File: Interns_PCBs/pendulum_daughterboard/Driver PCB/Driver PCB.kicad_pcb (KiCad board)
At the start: 2 copper layers, 69.2 x 54 mm, 43 parts, among them IC1 AND GATES, IC2 NAND (Used as AND), IC3 NAND (Used as Inverter), IC4 OR, IC5 MAX9928FAUA+, J1 AVR-ISP-6, J2 Coil, J4 Conn_01x04, J5 DRIVE_GND, J7 DRIVE_5V_IN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

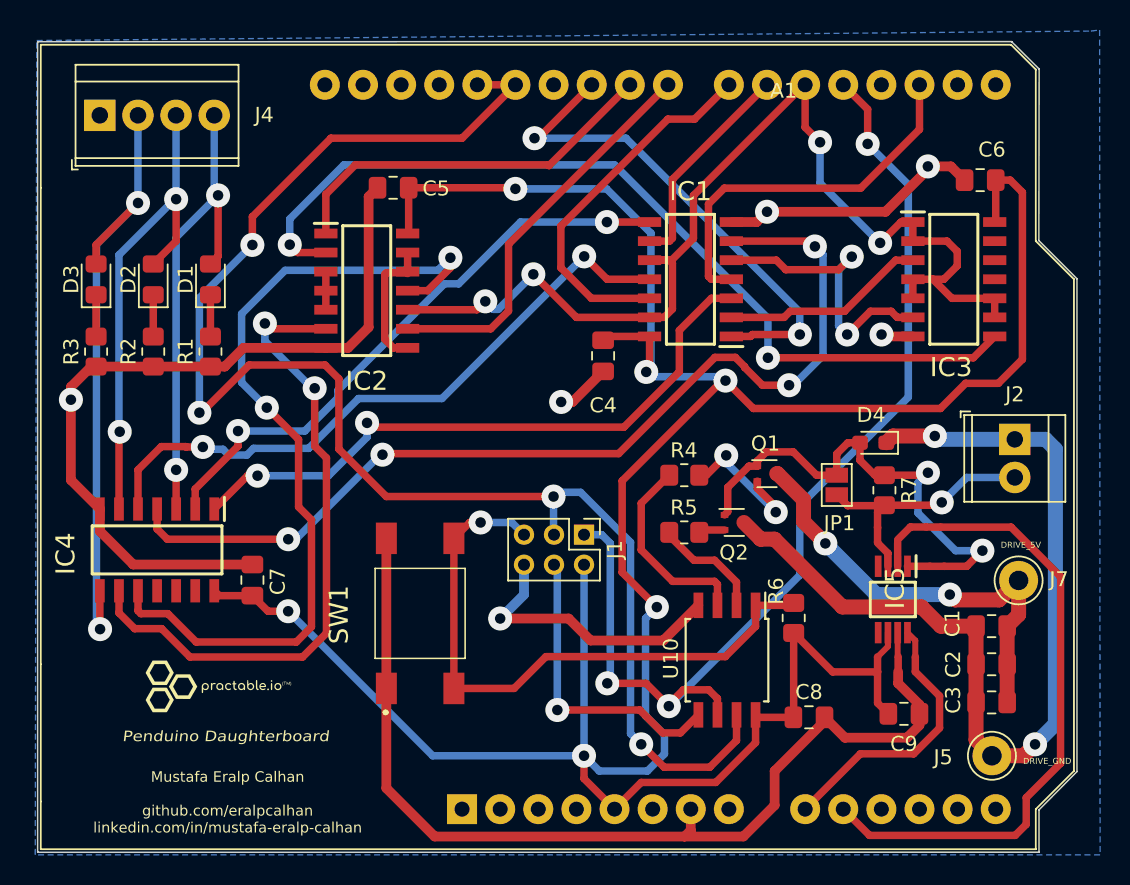
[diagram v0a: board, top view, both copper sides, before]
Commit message: Changed Diode
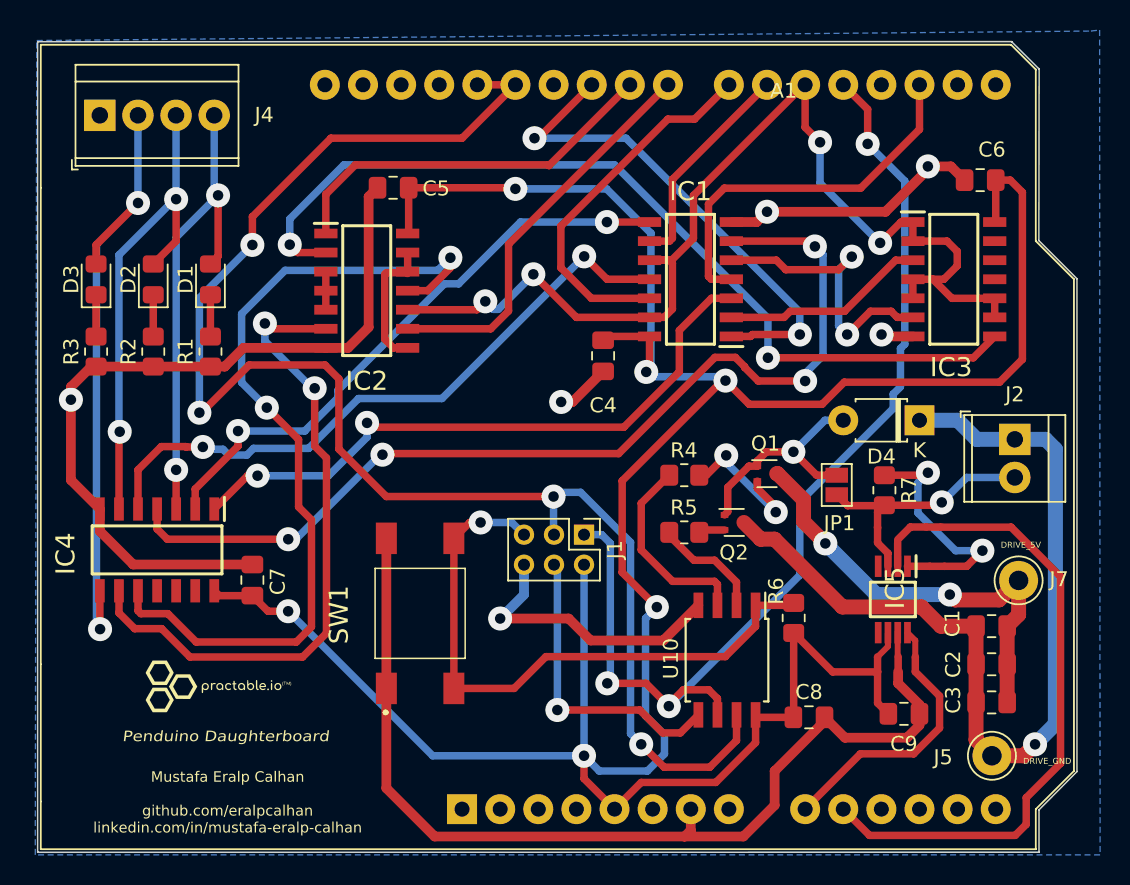
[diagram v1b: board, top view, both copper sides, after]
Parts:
- D4: footprint Diode_SMD:D_0603_1608Metric_Pad1.05x0.95mm_HandSolder -> Diode_THT:D_T-1_P5.08mm_Horizontal
- moved D4 3.43 mm to (149.9, 80.0)
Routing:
- net Net-(D4-Pad2): track 31.7 -> 29.4 mm, vias 2 -> 3
- net DRIVE_GND: track 62.6 -> 60.7 mm, vias 2 -> 1

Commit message: Changes with the Components
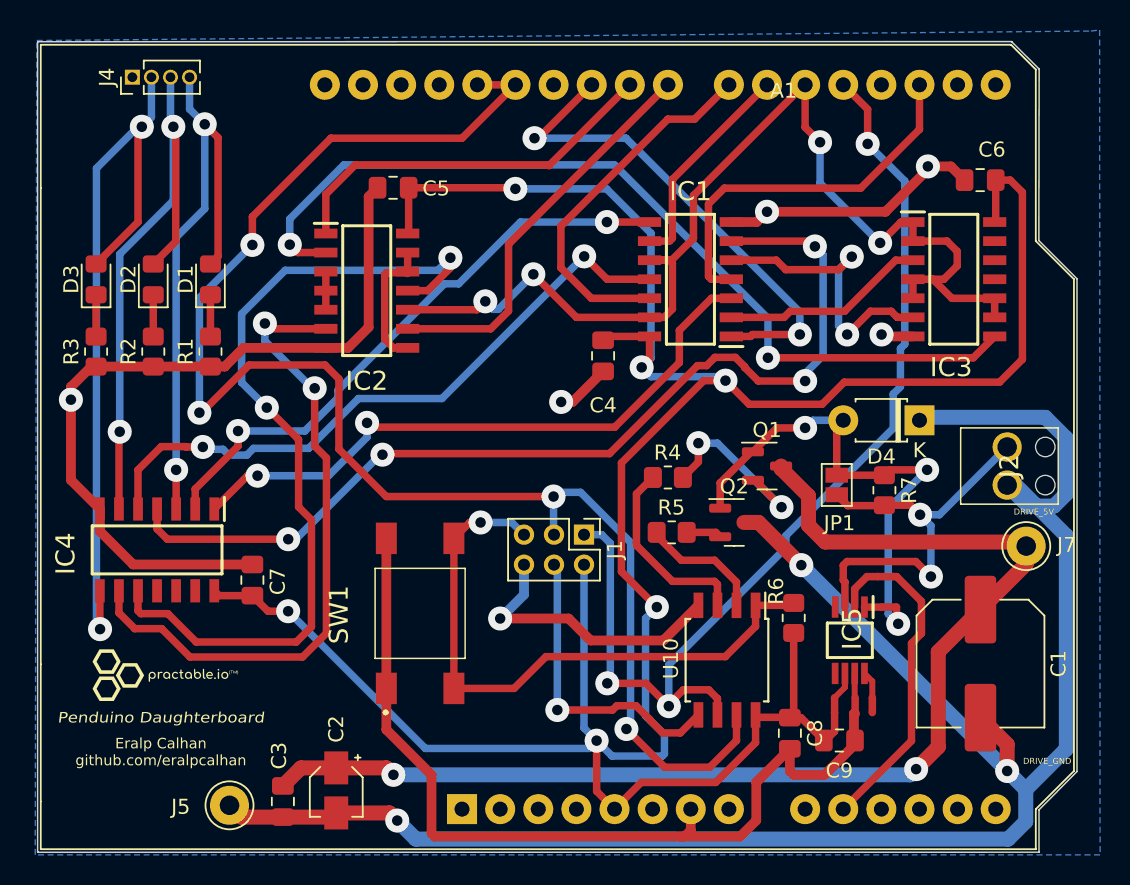
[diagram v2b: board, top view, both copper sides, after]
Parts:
- C1: value 460u -> 470u; footprint Capacitor_SMD:C_0805_2012Metric_Pad1.18x1.45mm_HandSolder -> Capacitor_SMD:C_Elec_8x10.2
- C2: footprint Capacitor_SMD:C_0805_2012Metric_Pad1.18x1.45mm_HandSolder -> Capacitor_SMD:CP_Elec_3x5.3
- J2: footprint TerminalBlock_TE-Connectivity:TerminalBlock_TE_282834-2_1x02_P2.54mm_Horizontal -> Connector_Molex:RSPROPenduinoTerminal
- J4: footprint TerminalBlock_TE-Connectivity:TerminalBlock_TE_282834-4_1x04_P2.54mm_Horizontal -> Connector_PinHeader_1.27mm:PinHeader_1x04_P1.27mm_Vertical
- Q1, Q2: footprint Package_TO_SOT_SMD:SOT-523 -> Package_TO_SOT_SMD:SOT-23
- moved J5 50.9 mm to (103.9, 105.7)
- moved C3 47.7 mm to (107.4, 105.4), turned to -90 degrees
- moved C2 44.5 mm to (111.0, 104.7), turned to -90 degrees
- moved C9 4.65 mm to (144.5, 101.3)
- moved NT3 4.62 mm to (147.6, 90.4)
- moved NT5 4.20 mm to (147.8, 92.5)
- moved NT1 3.95 mm to (144.2, 99.0)
- moved NT2 3.95 mm to (145.6, 99.0)
- moved NT6 3.95 mm to (146.7, 99.0)
- moved IC5 3.95 mm to (145.2, 94.7)
- moved G*** 3.62 mm to (99.6, 97.0)
- moved NT4 3.41 mm to (144.8, 90.2)
- moved J4 3.34 mm to (97.4, 57.1), turned to 90 degrees
- moved J2 3.09 mm to (155.7, 84.3), turned to 90 degrees
- moved C1 2.60 mm to (153.9, 96.2), turned to -90 degrees
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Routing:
- net DRIVE_GND: track 60.7 -> 129.6 mm, vias 1 -> 3
- net DRIVE_5V: track 29.4 -> 80.7 mm
- net CURRENT_SIGN_OUT: track 40.0 -> 18.6 mm
- net CURRENT_SENSE_OUT: track 15.6 -> 0.00 mm
- net Net-(J2-Pad2): track 14.6 -> 24.6 mm, vias 1 -> 2
- net OR_OUT_3: track 43.3 -> 51.1 mm
- net OR_OUT_1: track 32.3 -> 39.9 mm
- net OR_OUT_2: track 32.9 -> 39.9 mm
- net D_GND: track 160.2 -> 155.1 mm
- net Net-(D4-Pad2): track 29.4 -> 34.4 mm
- net D_5V: track 192.0 -> 188.2 mm
- net Net-(Q1-Pad2): track 10.1 -> 12.7 mm
- net LOAD_MCU: track 7.53 -> 8.36 mm
- net Net-(IC5-Pad2): track 3.83 -> 3.08 mm
- net Net-(Q2-Pad2): track 1.75 -> 2.35 mm
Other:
- board text added: "Eralp Calhan github.com/eralpcalhan"
- board text removed: "Mustafa Eralp Calhan github.com/eralpcalhan linkedin.com/in/mustafa-eralp-calhan"

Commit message: Friday Updates
24/06/22
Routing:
- net CURRENT_SENSE_OUT: track 0.00 -> 9.01 mm
- net D_GND: track 155.1 -> 153.7 mm
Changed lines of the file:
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@@
   (segment (start 95.25 87.400022) (end 97.468978 89.619) (width 0.65) (layer "F.Cu") (net 56))
   (segment (start 139.0142 66.802) (end 139.7 66.1162) (width 0.65) (layer "F.Cu") (net 56))
+  (segment (start 142.22252 102.89552) (end 141.224 101.897) (width 0.65) (layer "F.Cu") (net 56))
   (segment (start 93.3196 77.7878) (end 93.3196 78.6384) (width 0.65) (layer "F.Cu") (net 56))
   (segment (start 141.224 101.897) (end 138.984511 104.136489) (width 0.65) (layer "F.Cu") (net 56))
@@
   (segment (start 102.616 76.431) (end 98.806 76.431) (width 0.65) (layer "F.Cu") (net 56))
   (segment (start 117.348 103.632) (end 114.336 100.62) (width 0.65) (layer "F.Cu") (net 56))
-  (segment (start 145.5635 101.6031) (end 143.5346 103.632) (width 0.65) (layer "F.Cu") (net 56))
+  (segment (start 144.521089 102.645511) (end 144.27108 102.89552) (width 0.65) (layer "F.Cu") (net 56))
   (segment (start 94.996 76.431) (end 94.6764 76.431) (width 0.65) (layer "F.Cu") (net 56))
   (segment (start 95.25 85.921) (end 95.25 87.400022) (width 0.65) (layer "F.Cu") (net 56))
   (segment (start 114.336 100.62) (end 114.336 97.876) (width 0.65) (layer "F.Cu") (net 56))
   (segment (start 135.128 92.3405) (end 132.78502 94.68348) (width 0.65) (layer "F.Cu") (net 56))
-  (segment (start 141.224 103.378) (end 141.224 101.897) (width 0.65) (layer "F.Cu") (net 56))
-  (segment (start 143.5346 103.632) (end 141.478 103.632) (width 0.65) (layer "F.Cu") (net 56))
   (segment (start 97.468978 89.619) (end 105.41 89.619) (width 0.65) (layer "F.Cu") (net 56))
-  (segment (start 145.5635 101.346) (end 145.5635 101.6031) (width 0.65) (layer "F.Cu") (net 56))
   (segment (start 145.498089 99.560511) (end 145.5726 99.560511) (width 0.65) (layer "F.Cu") (net 56))
   (segment (start 126.48204 93.218) (end 127.94752 94.68348) (width 0.65) (layer "F.Cu") (net 56))
@@
   (segment (start 139.7 66.1162) (end 147.5994 66.1162) (width 0.65) (layer "F.Cu") (net 56))
   (segment (start 138.984511 104.136489) (end 138.984511 106.673738) (width 0.65) (layer "F.Cu") (net 56))
+  (segment (start 144.27108 102.89552) (end 142.22252 102.89552) (width 0.65) (layer "F.Cu") (net 56))
+  (segment (start 145.5635 101.346) (end 145.5635 101.732522) (width 0.65) (layer "F.Cu") (net 56))
   (segment (start 147.5994 66.1162) (end 150.4188 63.2968) (width 0.65) (layer "F.Cu") (net 56))
   (segment (start 151.9506 63.0936) (end 150.4188 63.0936) (width 0.65) (layer "F.Cu") (net 56))
@@
   (segment (start 145.4925 99.5661) (end 145.498089 99.560511) (width 0.65) (layer "F.Cu") (net 56))
   (segment (start 111.784022 75.184) (end 110.305 75.184) (width 0.65) (layer "F.Cu") (net 56))
-  (segment (start 141.478 103.632) (end 141.224 103.378) (width 0.65) (layer "F.Cu") (net 56))
   (segment (start 93.3196 83.9906) (end 93.3196 78.6384) (width 0.65) (layer "F.Cu") (net 56))
   (segment (start 147.456781 74.422) (end 147.329881 74.2951) (width 0.65) (layer "F.Cu") (net 56))
   (segment (start 132.78502 94.68348) (end 127.94752 94.68348) (width 0.65) (layer "F.Cu") (net 56))
+  (segment (start 144.650511 102.645511) (end 144.521089 102.645511) (width 0.65) (layer "F.Cu") (net 56))
   (segment (start 94.6764 76.431) (end 93.3196 77.7878) (width 0.65) (layer "F.Cu") (net 56))
   (segment (start 134.62 107.332213) (end 134.209702 107.742511) (width 0.65) (layer "F.Cu") (net 56))
+  (segment (start 145.5635 101.732522) (end 144.650511 102.645511) (width 0.65) (layer "F.Cu") (net 56))
   (segment (start 113.155969 73.812053) (end 111.784022 75.184) (width 0.65) (layer "F.Cu") (net 56))
   (segment (start 104.819334 75.184) (end 110.305 75.184) (width 0.65) (layer "F.Cu") (net 56))
@@
   (segment (start 123.508 91.63) (end 121.92 93.218) (width 0.65) (layer "B.Cu") (net 56))
   (segment (start 123.508 89.63) (end 123.508 91.63) (width 0.65) (layer "B.Cu") (net 56))
+  (segment (start 144.187969 103.970031) (end 145.165503 103.970031) (width 0.5) (layer "F.Cu") (net 57))
+  (segment (start 146.90052 102.235014) (end 146.90052 99.67092) (width 0.5) (layer "F.Cu") (net 57))
+  (segment (start 142.24 105.918) (end 144.187969 103.970031) (width 0.5) (layer "F.Cu") (net 57))
+  (segment (start 146.90052 99.67092) (end 146.7156 99.486) (width 0.5) (layer "F.Cu") (net 57))
+  (segment (start 145.165503 103.970031) (end 146.90052 102.235014) (width 0.5) (layer "F.Cu") (net 57))
   (segment (start 136.398 98.552) (end 136.398 99.6405) (width 0.5) (layer "F.Cu") (net 58))
   (segment (start 129.0575 97.536) (end 131.636666 97.536) (width 0.5) (layer "F.Cu") (net 58))
@@
   (segment (start 144.78 90.67) (end 144.892 90.782) (width 0.5) (layer "F.Cu") (net 63))
   (segment (start 144.892 90.782) (end 144.892 92.456) (width 0.5) (layer "F.Cu") (net 63))
-  (segment (start 149.327511 101.370489) (end 144.78 105.918) (width 0.5) (layer "F.Cu") (net 66))
-  (segment (start 149.989945 94.213391) (end 149.327511 94.875825) (width 0.5) (layer "F.Cu") (net 66))
-  (segment (start 149.989945 92.077945) (end 149.989945 94.213391) (width 0.5) (layer "F.Cu") (net 66))
-  (segment (start 148.074 90.424) (end 148.336 90.424) (width 0.5) (layer "F.Cu") (net 66))
-  (segment (start 148.336 90.424) (end 149.989945 92.077945) (width 0.5) (layer "F.Cu") (net 66))
-  (segment (start 149.327511 94.875825) (end 149.327511 101.370489) (width 0.5) (layer "F.Cu") (net 66))
+  (segment (start 146.464011 104.377511) (end 146.320489 104.377511) (width 0.5) (layer "F.Cu") (net 66))
+  (segment (start 149.989945 94.213391) (end 147.900031 96.303305) (width 0.5) (layer "F.Cu") (net 66))
+  (segment (start 148.074 90.424) (end 149.989945 92.339945) (width 0.5) (layer "F.Cu") (net 66))
+  (segment (start 146.320489 104.377511) (end 144.78 105.918) (width 0.5) (layer "F.Cu") (net 66))
+  (segment (start 147.900031 102.941491) (end 146.464011 104.377511) (width 0.5) (layer "F.Cu") (net 66))
+  (segment (start 149.989945 92.339945) (end 149.989945 94.213391) (width 0.5) (layer "F.Cu") (net 66))
+  (segment (start 147.900031 96.303305) (end 147.900031 102.941491) (width 0.5) (layer "F.Cu") (net 66))
   (segment (start 144.892 97.803) (end 144.201 98.494) (width 0.4) (layer "F.Cu") (net 67))
   (segment (start 144.892 96.88) (end 144.892 97.803) (width 0.4) (layer "F.Cu") (net 67))

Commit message: 01/07 UPDATES
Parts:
- J4: footprint Connector_PinHeader_1.27mm:PinHeader_1x04_P1.27mm_Vertical -> Connector_PinHeader_2.54mm:PinHeader_1x04_P2.54mm_Vertical
- moved J4 1.14 mm to (96.4, 57.6)
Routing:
- net OR_OUT_1: track 39.9 -> 39.2 mm

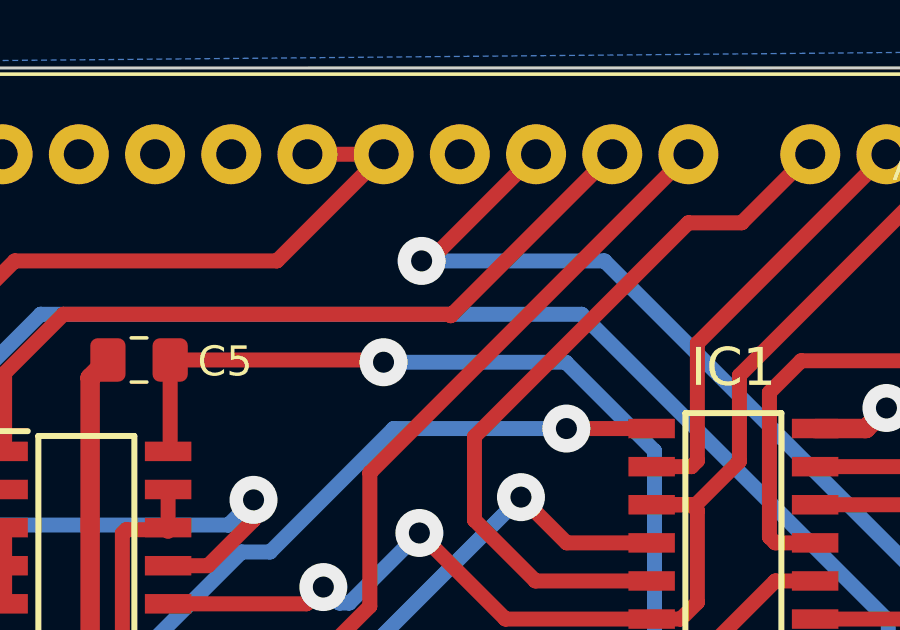
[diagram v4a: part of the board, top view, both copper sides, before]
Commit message: Pull down and Current Limiting Resistors
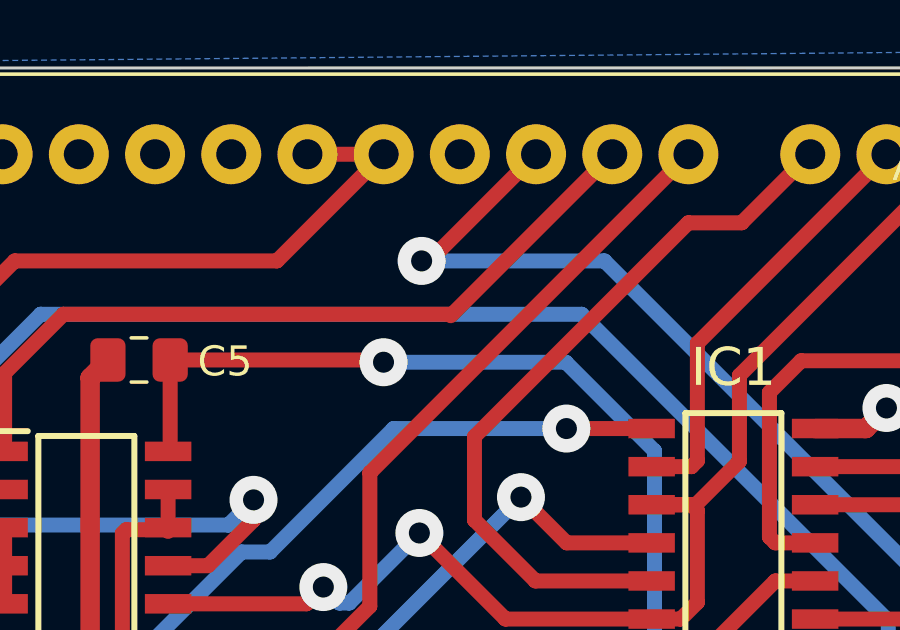
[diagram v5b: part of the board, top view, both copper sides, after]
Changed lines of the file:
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@@
   (segment (start 133.096 59.944) (end 125.96752 67.07248) (width 0.5) (layer "F.Cu") (net 16))
   (segment (start 125.96752 67.07248) (end 125.96752 69.85) (width 0.5) (layer "F.Cu") (net 16))
-  (segment (start 125.12704 62.992) (end 125.17652 63.04148) (width 0.5) (layer "F.Cu") (net 17))
   (segment (start 110.305 64.955) (end 112.268 62.992) (width 0.5) (layer "F.Cu") (net 17))
   (segment (start 130.56 57.658) (end 125.17652 63.04148) (width 0.5) (layer "F.Cu") (net 17))
@@
       0b373cb6-494f-4c34-8ef3-e4c5a251e602
       0bb85e61-84e1-4c41-b056-cde6ef24aa7d
-      0be48bb9-2cb3-4ce5-8dd1-002f1bf19f14
       0beb3824-45f4-46aa-b785-c3b38e34fdde
       0ca060f0-d89f-4be6-8660-8f276045301e
